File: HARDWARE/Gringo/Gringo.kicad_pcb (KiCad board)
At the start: 2 copper layers, 201 x 48 mm, 64 parts, among them J1 Conn_01x06, J10 Conn_01x06, J11 Conn_01x06, J12 Conn_01x06, J13 Conn_01x06, J14 Conn_01x06, J15 Conn_01x06, J16 Conn_01x06, J17 Conn_01x05_Pin, J2 Conn_01x06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

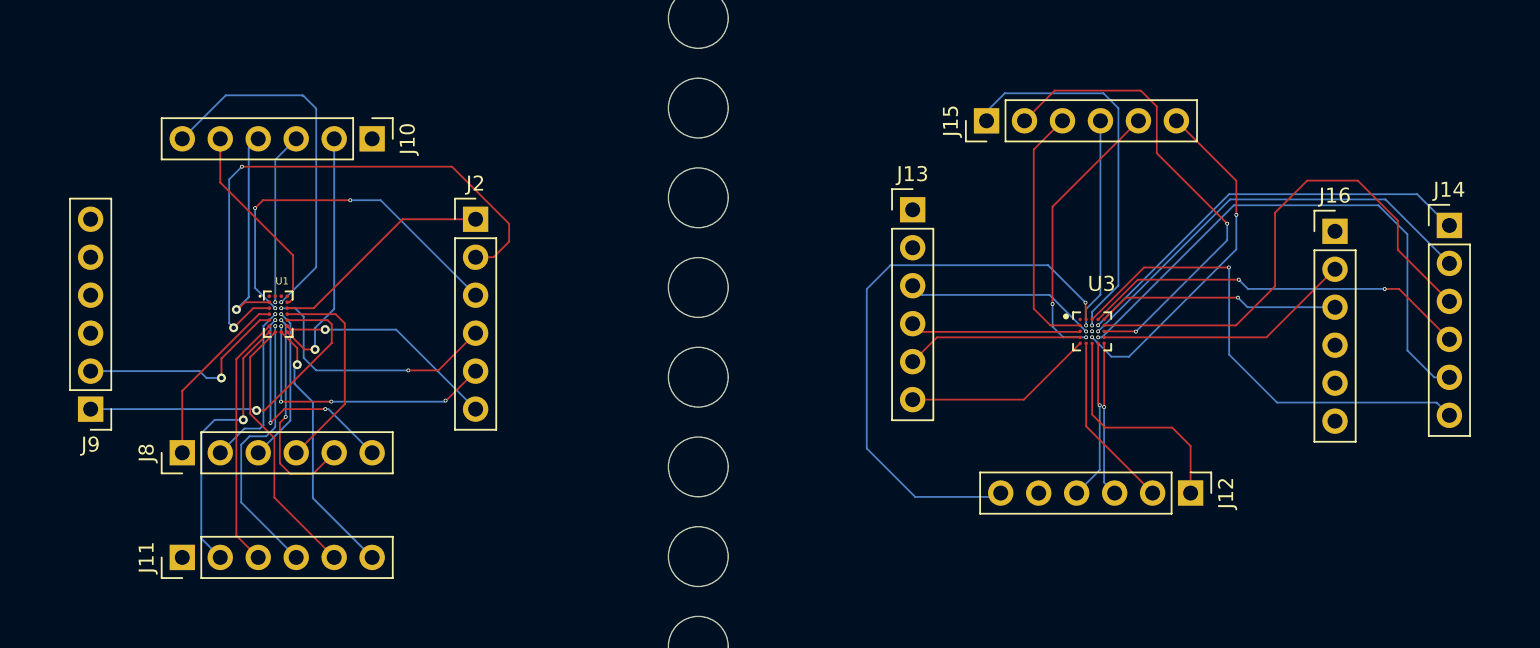
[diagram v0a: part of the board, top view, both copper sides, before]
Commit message: Correction before buy JLCPCB
Remove of via down to 2 tiny component
Change of clearance of the pads to pass routes
To remove clearance : select all the pads > propriétés > Clearance Overrides and DON T PUT 0 (herited) but something like -0.001
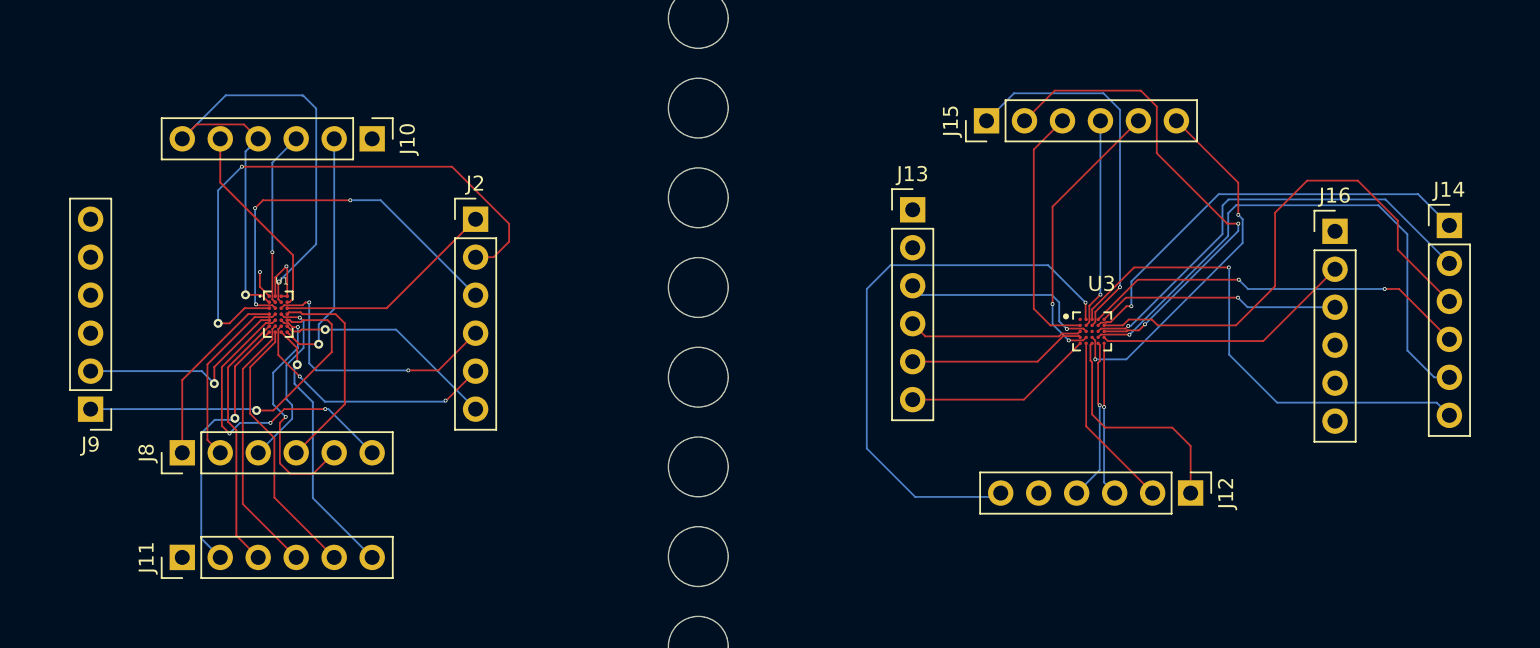
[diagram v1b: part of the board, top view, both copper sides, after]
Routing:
- net GND: track 67.2 -> 73.8 mm, vias 10 -> 12
- net Net-(J8-Pin_6): track 15.4 -> 20.9 mm
- net Net-(J10-Pin_4): track 38.9 -> 43.1 mm
- net Net-(J8-Pin_5): track 14.4 -> 16.1 mm
- net Net-(J8-Pin_3): track 10.4 -> 12.0 mm
- net Net-(J2-Pin_5): track 18.9 -> 17.3 mm, vias 4 -> 2
- net Net-(J15-Pin_6): track 23.4 -> 24.7 mm
- net Net-(J14-Pin_2): track 28.9 -> 30.0 mm
- net Net-(J15-Pin_2): track 31.8 -> 32.9 mm
- net Net-(J2-Pin_4): track 17.4 -> 18.5 mm
- net Net-(J14-Pin_1): track 28.0 -> 29.0 mm
- net Net-(J14-Pin_5): track 36.5 -> 37.4 mm
- net Net-(J2-Pin_2): track 37.5 -> 38.3 mm
- net Net-(J8-Pin_2): track 11.5 -> 12.2 mm, vias 1 -> 0
- net Net-(J13-Pin_3): track 12.9 -> 13.6 mm
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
